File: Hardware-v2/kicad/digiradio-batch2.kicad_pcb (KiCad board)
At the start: 6 copper layers, 60 x 80 mm, 167 parts, among them J1 USB_C_Receptacle_USB2.0_16P, J2 RF/COAXIAL SMA BHD JACK STR 5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, J3 BAT, U1 24AA025E64, U10 BQ25896RTWT, U11 TPS63031DSKR, U12 TPS7A2018PDBVR, U13 ADAU1452, U14 25AA1024-I_SM, U2 ESP32-S31-WROOM-3, U3 W25Q128JVS, U4 TLV62568DBV, U5 TPS63031DSKR, U6 FSC-BT1058, U7 W25Q16JW, U8 Si4684-A10-GM, U9 MAX17048G_T10, Y2 ABM8-19.200MHZ-10-1-U-T, Y3 ABM3B-12.288MHZ-10-1-U-T

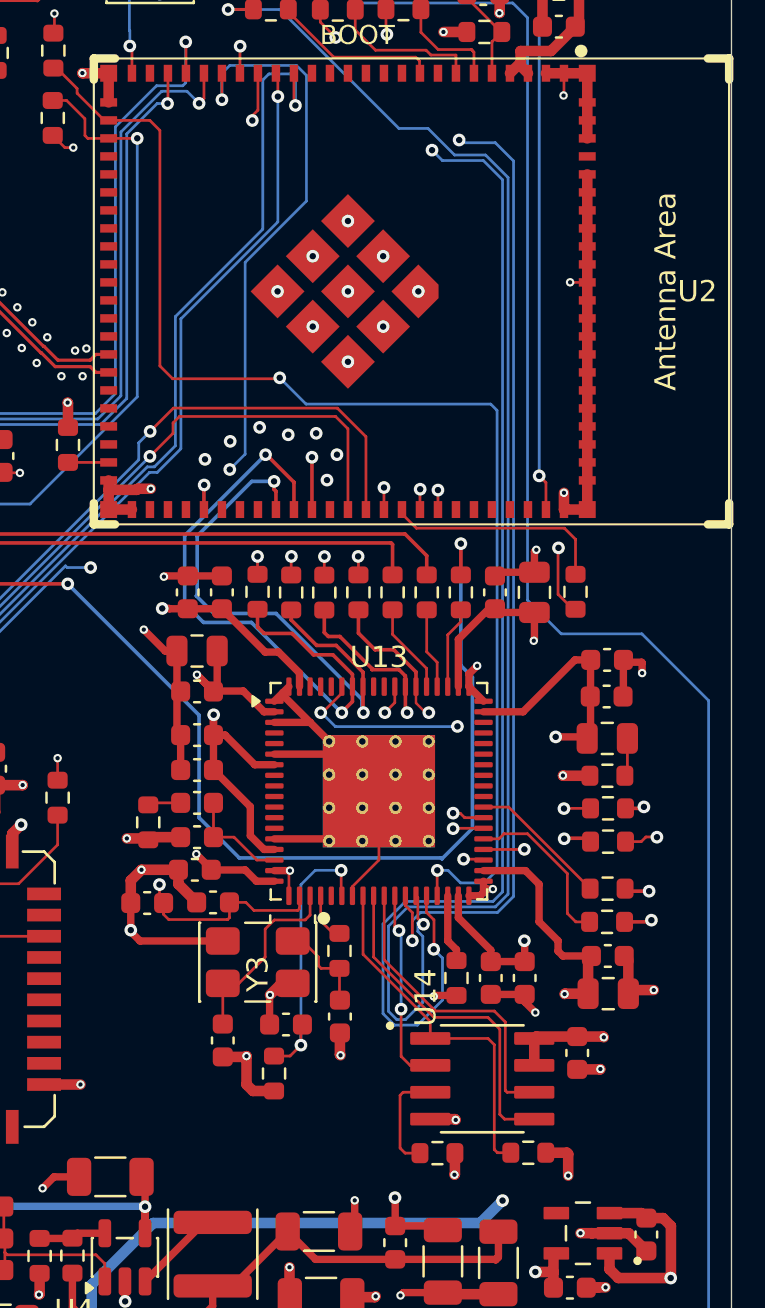
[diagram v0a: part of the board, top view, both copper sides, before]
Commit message: Correct the v2 EEPROM footprint and crystal load capacitors
Compared the ADAU1452 section with the EVAL-ADAU1452REVBZ user guide
(UG-1662) and the ADAU1452 datasheet.

- U14: 25AA1024-I/SM is a 208 mil SOIJ-8, but it was on a 150 mil SOIC
  footprint. Use Package_SO:SOIC-8_5.3x5.3mm_P1.27mm and fix the PNM.
- C141/C142 (Y3): 15 pF NP0 instead of 12 pF X7R.
- C139/C140 (Y2): 12 pF NP0 instead of 12 pF X7R.
- C6: add 1 uF on 1V2 near U13 pin 20, which the datasheet asks for.
- Widen the 1V2 trace from U13 pin 20 to 0.35 mm.

Co-Authored-By: Claude Opus 5.5 (1M context) <noreply@anthropic.com>
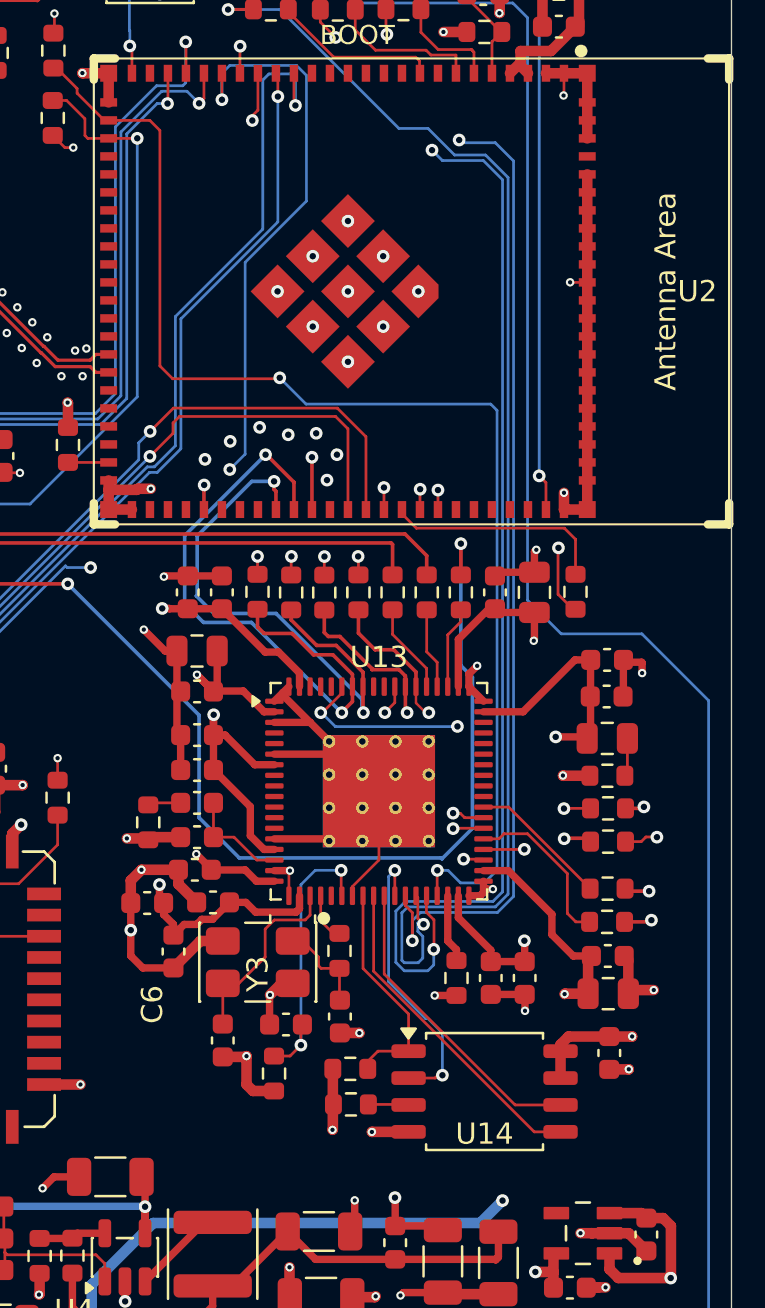
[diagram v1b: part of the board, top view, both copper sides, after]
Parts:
- added C6: 1uF, Capacitor_SMD:C_0603_1608Metric, F.Cu at (58.6, 152.1)
- C141, C142: value 12pF -> 15pF
- U14: value 25AA1024-I_SM -> 25AA1024-I/SM; footprint MIKILAB_25AA1024:SOIC127P600X175-8N -> Package_SO:SOIC-8_5.3x5.3mm_P1.27mm
- moved R35 9.29 mm to (67.0, 157.7), turned to 180 degrees
- moved R34 4.69 mm to (67.0, 159.3), turned to 180 degrees
- moved C32 1.52 mm to (79.2, 156.9)
- moved U14 0.61 mm to (73.3, 158.7)
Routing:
- net /AudioDomain/SS_M: track 17.0 -> 10.7 mm
- net SPI_MOSI: track 122.7 -> 116.8 mm
- net SPI_SCLK: track 122.6 -> 116.9 mm
- net /AudioDomain/MISO_M: track 9.26 -> 13.8 mm
- net Net-(U14-~{WP}): track 5.02 -> 1.91 mm
- net GND: track 260.1 -> 261.7 mm
- net 3V3_AUDIO: track 126.9 -> 126.4 mm, vias 15 -> 14
- net 1V2: track 119.2 -> 119.8 mm

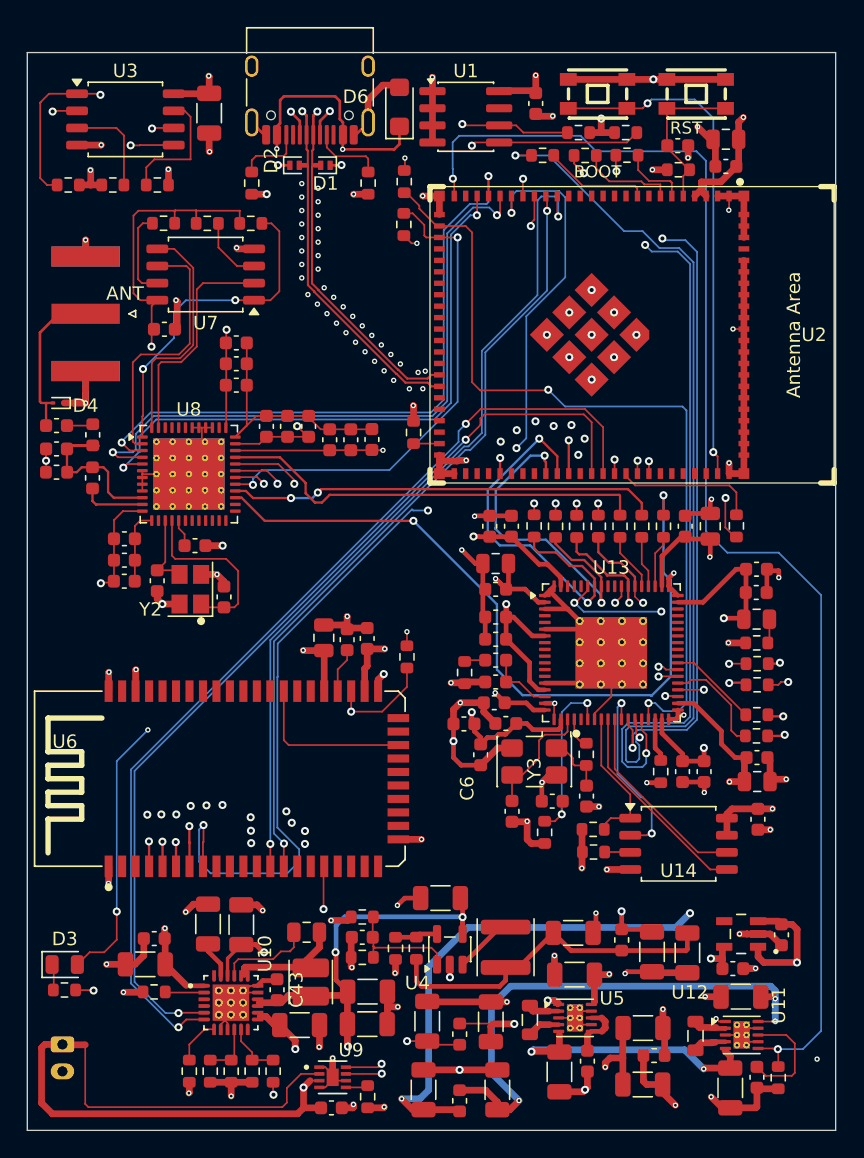
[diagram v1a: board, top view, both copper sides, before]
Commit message: Add the TOSLINK output to the v2 board
Fit an Everlight PLT237/T10WH as J5 on the top edge, driven from
ADAU1452 SPDIFOUT through R56, with FB3 and C65 on its 3V3_AUDIO
supply. The optical face sits 2.31 mm past the board edge.

Move flash U3 and its parts next to U8 and U13 to free the edge, which
shortens the M_SPI traces from 80-95 mm to 34-46 mm.

Pin order follows the LCSC footprint: pad 1 Vin, 2 Vcc, 3 GND.

Co-Authored-By: Claude <noreply@anthropic.com>
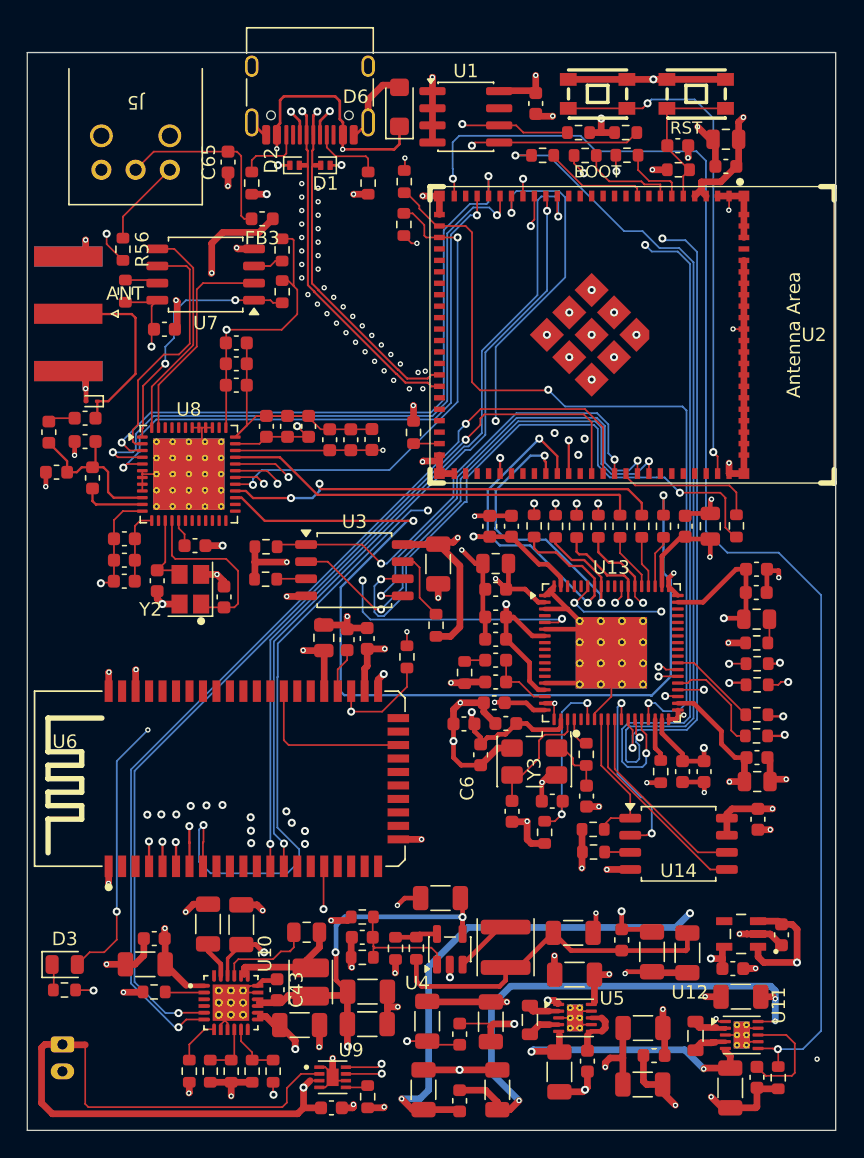
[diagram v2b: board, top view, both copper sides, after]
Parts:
- removed D4: ESD9B5.0ST5G, Diode_SMD:D_SOD-923
- added C65: 100nF, Capacitor_SMD:C_0603_1608Metric, F.Cu at (39.9, 108.1)
- added D5: ESD9L5.0ST5G, Diode_SMD:D_SOD-923, F.Cu at (29.8, 125.9)
- added FB3: BLM18SG121TN1D, Inductor_SMD:L_0603_1608Metric, F.Cu at (42.4, 112.3)
- added J5: PLT237/T10WH, MIKILAB_FCR684205R:PLT237_T10WH, F.Cu at (35.6, 108.7)
- added R56: 33, Resistor_SMD:R_0603_1608Metric, F.Cu at (32.1, 114.6)
- C141, C142: value 15pF -> 12pF
- moved R10 38.7 mm to (55.3, 142.5), turned to 90 degrees
- moved C5 37.5 mm to (55.5, 138.0)
- moved U3 37.5 mm to (49.3, 138.4)
- moved R9 31.4 mm to (42.7, 139.1)
- moved R31 30.6 mm to (42.7, 136.7), turned to 180 degrees
- moved R14 5.89 mm to (43.9, 114.7), turned to 90 degrees
- moved R15 5.78 mm to (32.3, 117.7), turned to -90 degrees
- moved R32 5.58 mm to (43.9, 117.8), turned to 90 degrees
- moved L1 3.27 mm to (26.6, 128.2)
- moved C20 2.19 mm to (29.3, 127.1), turned to 180 degrees
- moved C22 2.19 mm to (29.3, 128.9)
- moved J2 1.29 mm to (28.0, 119.4)
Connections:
- U13 pad 5: unconnected-(U13-SPDIFOUT-Pad5) -> /AudioDomain/SPDIFOUT
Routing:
- net /AudioDomain/SPDIFOUT: track 0.00 -> 56.5 mm, vias 0 -> 3
- net /Esp32-S31/M_SPI_SCLK: track 95.5 -> 45.8 mm
- net /Esp32-S31/M_SPI_MOSI: track 81.1 -> 32.5 mm
- net /Esp32-S31/M_SPI_CS#: track 83.2 -> 34.9 mm
- net /Esp32-S31/M_SPI_MISO: track 80.1 -> 39.4 mm
- net 3V3_DIGITAL: track 158.7 -> 185.4 mm, vias 11 -> 10
- net Net-(J5-VCC): track 0.00 -> 13.8 mm
- net I2S_RADIO_IN_BCLK: track 57.0 -> 69.5 mm
- net 3V3_AUDIO: track 126.4 -> 133.7 mm, vias 14 -> 15
- net 1V8_SI4684: track 150.3 -> 143.8 mm
- net Net-(J5-VIN): track 0.00 -> 6.52 mm
- net /Radio Domain/NV_SSB: track 24.7 -> 18.7 mm
- net Net-(U3-IO2): track 7.39 -> 2.19 mm
- net Net-(U7-IO3): track 6.57 -> 2.47 mm
- net Net-(U3-IO3): track 9.44 -> 5.40 mm
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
